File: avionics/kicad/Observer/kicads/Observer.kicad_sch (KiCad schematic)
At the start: 66 parts, among them Q1 AO3400 logic-level N-MOSFET, T1 Wurth 749010012A, T1_CMC1 SRF2012-100Y, T1_CMC2 SRF2012-100Y, T1_D1 PRTR5V0U2X, T1_D2 PRTR5V0U2X, T2 Wurth 749010012A, T2_CMC1 SRF2012-100Y, T2_CMC2 SRF2012-100Y, T2_D1 PRTR5V0U2X, T2_D2 PRTR5V0U2X, U2 Microchip KSZ9477, U3 TI MSPM0G3519-Q1, U4 TI ISOW1044BDFMR, U5 Infineon SLB 9672AU2.0, U6 TI ISOW1412, Y1 25MHz

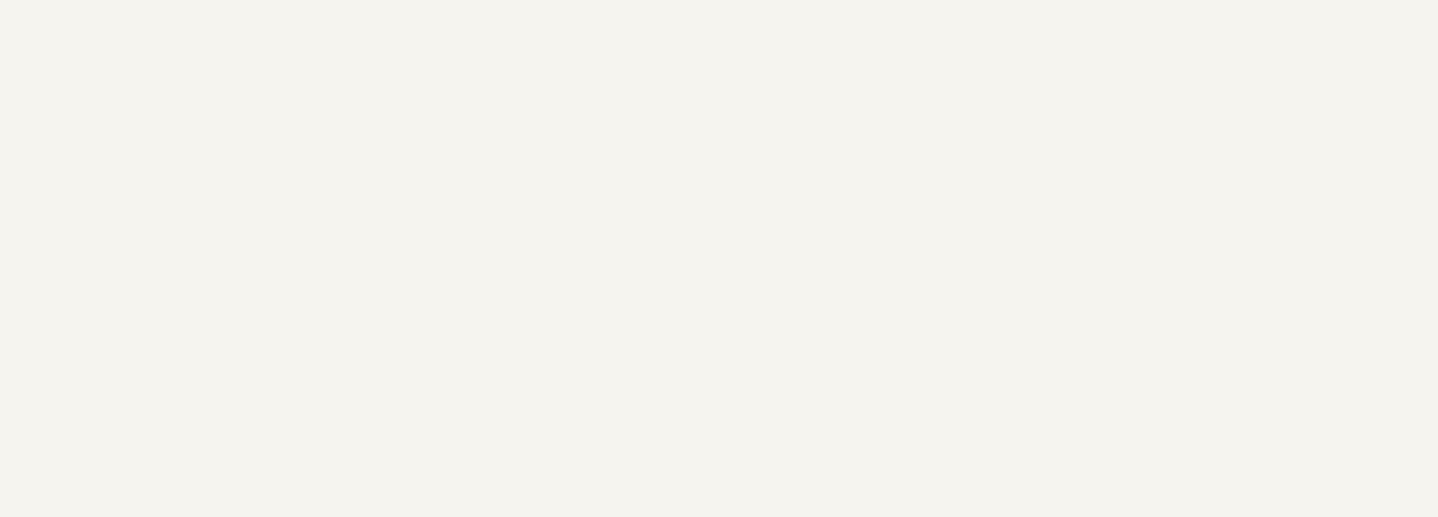
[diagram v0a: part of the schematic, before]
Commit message: docs(avionics): Wurth usage notice + uncrewed-only statement on 5 boards; catalogue REF-SENSOR-022..040
Owner decision 2026-09-26: retain the Wurth parts. The Wurth datasheet
usage notice is quoted verbatim [REF-SENSOR-028: Wurth 749010012A data
sheet rev 004.000 p.1] with an 'intended for use only on uncrewed
aircraft' statement in each Wurth-bearing board's .md, as a schematic
text item and PCB Cmts.User text, and in title-block comments 8/9
(tools/add_board_notices.py, idempotent). ERC/DRC/parity counts
unchanged on all five boards (kicad-cli 9.0.2).

REFERENCES.md: REF-SENSOR-022/023/025-030/033/038/040 were cited by
board schematics and generator scripts but never catalogued; entries
added with URLs validated 2026-09-26, unreachable ones marked
'requires verification'.

AI-authored: Claude Opus 5.5 (Anthropic).

Co-Authored-By: Claude Opus 5.5 <noreply@anthropic.com>
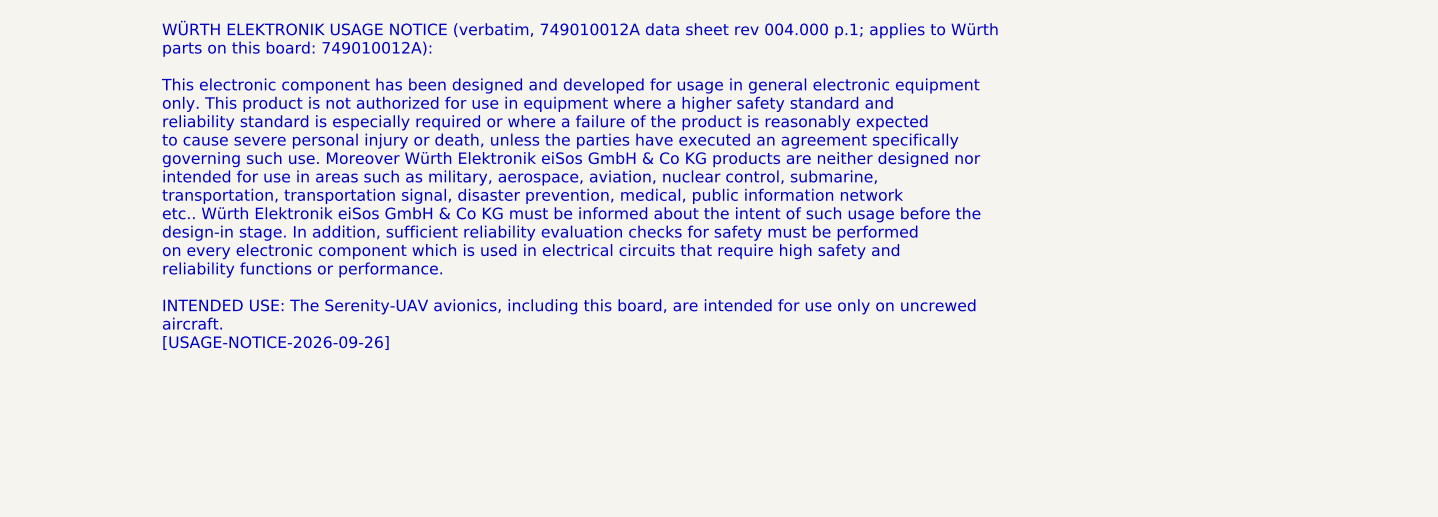
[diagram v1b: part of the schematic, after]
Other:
- note added: "WÜRTH ELEKTRONIK USAGE NOTICE (verbatim, 749010012A data sheet rev 004.000 p.1; applies to Würth parts on this board: 749010012A): This electronic component has been designed and developed for usage in general electronic equipment only. This product is not authorized for use in equipment where a higher safety standard and reliability standard is especially required or where a failure of the produ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"
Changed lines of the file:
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@@
     (comment 3 "License: CC BY 4.0  |  creativecommons.org/licenses/by/4.0")
     (comment 4 "SoM carrier: real clean-room symbols; see gen_Observer_carrier_sch.py")
-  )
+		(comment 8 "Wurth parts (749010012A): see Wurth usage notice on this page [USAGE-NOTICE-2026-09-26]")
+		(comment 9 "Intended for use ONLY on uncrewed aircraft")
+	)
   (text "OBSERVER — Nose/Cargo Vision/ToF/Laser  |  STANDALONE board (NOT a PB2-I cape)  |  SoM end-state: PHYTEC PCM-071 + carrier (KSZ9477 / MSPM0G3519-Q1 / SLB9672 / ISOW1044)" (at 10.00 8.00 0)
     (effects (font (size 2.00 2.00)))
@@
     (property "Intersheet References" "${INTERSHEET_REFS}" (at 137.16 195.58 0)
       (effects (font (size 1.016 1.016)) (hide yes))))
-)
+	(text "WÜRTH ELEKTRONIK USAGE NOTICE (verbatim, 749010012A data sheet rev 004.000 p.1; applies to Würth\nparts on this board: 749010012A):\n\nThis electronic component has been designed and developed for usage in general electronic equipment\nonly. This product is not authorized for use in equipment where a higher safety standard and\nreliability standard is especially required or where a failure of the product is reasonably expected\nto cause severe personal injury or death, unless the parties have executed an agreement specifically\ngoverning such use. Moreover Würth Elektronik eiSos GmbH & Co KG products are neither designed nor\nintended for use in areas such as military, aerospace, aviation, nuclear control, submarine,\ntransportation, transportation signal, disaster prevention, medical, public information network\netc.. Würth Elektronik eiSos GmbH & Co KG must be informed about the intent of such usage before the\ndesign-in stage. In addition, sufficient reliability evaluation checks for safety must be performed\non every electronic component which is used in electrical circuits that require high safety and\nreliability functions or performance.\n\nINTENDED USE: The Serenity-UAV avionics, including this board, are intended for use only on uncrewed\naircraft.\n[USAGE-NOTICE-2026-09-26]"
+		(exclude_from_sim no)
+		(at -35.56 -114.30 0)
+		(effects (font (size 1.27 1.27)) (justify left top))
+	)
+	)

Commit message: fix(avionics): TLV62569 -> TLV62569PDRLR and TLV75725 -> TLV75725PDRVR package swaps; regulator circuit fixes; stale-component cleanup
Owner-approved swaps (2026-09-26, avionics/WBS.md U7.1e) using the
datasheet-verified SecureControllers library via ${SECURE_CONTROLLERS_LIB}:
- CAN-PERIPH-GW-1 U_REG_3V3, Observer U_REG_3V3/U_REG_1V2, Flight
  Engineer U_REG_3V3_H -> TLV62569PDRLR (SOT-563, 1.6 x 1.6 mm).
  Pins remapped by name; the old symbols had FB/PG swapped (gateway,
  Observer) or sat on a 3-pad SOT-23 (Flight Engineer).
- Observer U_REG_2V5 -> TLV75725PDRVR (WSON-6 2x2, EP to GND).
- Feedback dividers per TLV62569 Sec. 8.2.2.2 Eq. 2 (VFB 0.6 V):
  gateway 10k/20k (0.9 V!) -> 453k/100k = 3.318 V; Observer placeholders
  -> 453k/100k (3V3) and 100k/100k (1V2).
- Flight Engineer: EN was tied to its own 3V3 output and FB straight to
  +3V3 (would regulate at 0.6 V); EN -> +5V, added R_H_FBT 453k /
  R_H_FBB 100k. Parity 2 -> 0, ERC 0.
- tools/kicad_prune_stale.py: parity-driven removal of stale electrical
  footprints and only the copper they orphan; mounting holes are marked
  board_only + renumbered (Commo parity 93 -> 86, Observer 21 -> 17).
- New tools kicad_relink.py / kicad_add_part.py / kicad_set_value.py;
  SecureControllers entries added to every board's lib tables.

Sources: TI TLV62569 (SLVSDG1C) Pin Functions, Sec. 8.2.2.2; TI TLV757P
Fig. 4-3, Pin Functions, DRV0006A.

AI-authored: Claude Opus 5.5 (Anthropic).

Co-Authored-By: Claude Opus 5.5 <noreply@anthropic.com>
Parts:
- R_FB1B, R_FB3B: value R_fbbot -> 100k 1%
- R_FB1T: value R_fbtop -> 100k 1%
- R_FB3T: value R_fbtop -> 453k 1%
- U_REG_1V2: value TLV62569 -> +1V2 -> TLV62569PDRLR; footprint Package_TO_SOT_SMD:SOT-23-6 -> Package_TO_SOT_SMD:SOT-563; symbol TLV62569_DBV -> SecureControllers:TLV62569PDRL
- U_REG_2V5: value TLV75725 -> +2V5 -> TLV75725PDRVR; footprint Package_TO_SOT_SMD:SOT-23-5 -> Package_SON:WSON-6-1EP_2x2mm_P0.65mm_EP1x1.6mm; symbol TLV75725_DBV -> SecureControllers:TLV75725PDRV
- U_REG_3V3: value TLV62569 -> +3V3 -> TLV62569PDRLR; footprint Package_TO_SOT_SMD:SOT-23-6 -> Package_TO_SOT_SMD:SOT-563; symbol TLV62569_DBV -> SecureControllers:TLV62569PDRL
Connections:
- net +2V5: now also U_REG_2V5.1 (OUT); no longer U_REG_2V5.5 (OUT)
- net +3V3: now also U_REG_2V5.4 (EN), U_REG_2V5.6 (IN); no longer U_REG_2V5.1 (IN), U_REG_2V5.3 (EN)
- net +5V: now also U_REG_1V2.3 (VIN), U_REG_1V2.5 (EN), U_REG_3V3.3 (VIN), U_REG_3V3.5 (EN); no longer U_REG_1V2.1 (EN), U_REG_1V2.4 (VIN), U_REG_3V3.1 (EN), U_REG_3V3.4 (VIN)
- net GND: now also U_REG_2V5.3 (GND), U_REG_2V5.7 (EP); no longer U_REG_2V5.2 (GND)
- net U_REG_1V2_FB: now also U_REG_1V2.1 (FB); no longer U_REG_1V2.5 (FB)
- net U_REG_1V2_SW: now also U_REG_1V2.4 (SW); no longer U_REG_1V2.3 (SW)
- net U_REG_3V3_FB: now also U_REG_3V3.1 (FB); no longer U_REG_3V3.5 (FB)
- net U_REG_3V3_SW: now also U_REG_3V3.4 (SW); no longer U_REG_3V3.3 (SW)
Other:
- moved on the sheet: U_REG_1V2, U_REG_3V3
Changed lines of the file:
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@@
     (property "Intersheet References" "${INTERSHEET_REFS}" (at 19.92 33.27 0)
       (effects (font (size 1.016 1.016)) (hide yes))))
-  (symbol (lib_id "TLV62569_DBV") (at 25.00 48.00 0)
+  (symbol (lib_id "SecureControllers:TLV62569PDRL") (at 25.00 48.00 0)
     (unit 1) (exclude_from_sim no) (in_bom yes) (on_board yes) (dnp no)
     (property "Reference" "U_REG_3V3" (at 25.00 44.19 0)
       (effects (font (size 1.27 1.27))))
-    (property "Value" "TLV62569 -> +3V3" (at 25.00 51.81 0)
-      (effects (font (size 1.27 1.27))))
-    (property "Footprint" "Package_TO_SOT_SMD:SOT-23-6" (at 0 0 0)
-      (effects (font (size 1.27 1.27)) (hide yes)))
-    (property "Datasheet" "" (at 0 0 0)
-      (effects (font (size 1.27 1.27)) (hide yes)))
-  )
-  (global_label "+5V" (shape bidirectional) (at 17.38 45.46 180)
+    (property "Value" "TLV62569PDRLR" (at 25.00 51.81 0)
+      (effects (font (size 1.27 1.27))))
+    (property "Footprint" "Package_TO_SOT_SMD:SOT-563" (at 0 0 0)
+      (effects (font (size 1.27 1.27)) (hide yes)))
+    (property "Datasheet" "https://www.ti.com/lit/ds/symlink/tlv62569.pdf" (at 0 0 0)
+      (effects (font (size 1.27 1.27)) (hide yes)))
+  )
+  (global_label "+5V" (shape bidirectional) (at 14.8400 45.4600 180)
     (effects (font (size 1.016 1.016)))
     (property "Intersheet References" "${INTERSHEET_REFS}" (at 17.38 45.46 0)
       (effects (font (size 1.016 1.016)) (hide yes))))
-  (global_label "GND" (shape bidirectional) (at 17.38 48.00 180)
+  (global_label "GND" (shape bidirectional) (at 25.0000 58.1600 270)
     (effects (font (size 1.016 1.016)))
     (property "Intersheet References" "${INTERSHEET_REFS}" (at 17.38 48.00 0)
       (effects (font (size 1.016 1.016)) (hide yes))))
-  (global_label "+5V" (shape bidirectional) (at 17.38 50.54 180)
+  (global_label "+5V" (shape bidirectional) (at 14.8400 42.9200 180)
     (effects (font (size 1.016 1.016)))
     (property "Intersheet References" "${INTERSHEET_REFS}" (at 17.38 50.54 0)
       (effects (font (size 1.016 1.016)) (hide yes))))
-  (global_label "U_REG_3V3_SW" (shape bidirectional) (at 32.62 45.46 0)
+  (global_label "U_REG_3V3_SW" (shape bidirectional) (at 35.1600 42.9200 0)
     (effects (font (size 1.016 1.016)))
     (property "Intersheet References" "${INTERSHEET_REFS}" (at 32.62 45.46 0)
       (effects (font (size 1.016 1.016)) (hide yes))))
-  (global_label "U_REG_3V3_FB" (shape bidirectional) (at 32.62 48.00 0)
+  (global_label "U_REG_3V3_FB" (shape bidirectional) (at 35.1600 45.4600 0)
     (effects (font (size 1.016 1.016)))
     (property "Intersheet References" "${INTERSHEET_REFS}" (at 32.62 48.00 0)
       (effects (font (size 1.016 1.016)) (hide yes))))
-  (global_label "+3V3_PG" (shape bidirectional) (at 32.62 50.54 0)
+  (global_label "+3V3_PG" (shape bidirectional) (at 35.1600 48.0000 0)
     (effects (font (size 1.016 1.016)))
     (property "Intersheet References" "${INTERSHEET_REFS}" (at 32.62 50.54 0)
@@
     (property "Reference" "R_FB3T" (at 45.00 50.19 0)
       (effects (font (size 1.27 1.27))))
-    (property "Value" "R_fbtop" (at 45.00 57.81 0)
+    (property "Value" "453k 1%" (at 45.00 57.81 0)
       (effects (font (size 1.27 1.27))))
     (property "Footprint" "Resistor_SMD:R_0402_1005Metric" (at 0 0 0)
@@
     (property "Reference" "R_FB3B" (at 45.00 55.19 0)
       (effects (font (size 1.27 1.27))))
-    (property "Value" "R_fbbot" (at 45.00 62.81 0)
+    (property "Value" "100k 1%" (at 45.00 62.81 0)
       (effects (font (size 1.27 1.27))))
     (property "Footprint" "Resistor_SMD:R_0402_1005Metric" (at 0 0 0)
@@
     (property "Intersheet References" "${INTERSHEET_REFS}" (at 12.81 48.00 0)
       (effects (font (size 1.016 1.016)) (hide yes))))
-  (symbol (lib_id "TLV62569_DBV") (at 25.00 70.00 0)
+  (symbol (lib_id "SecureControllers:TLV62569PDRL") (at 25.00 70.00 0)
     (unit 1) (exclude_from_sim no) (in_bom yes) (on_board yes) (dnp no)
     (property "Reference" "U_REG_1V2" (at 25.00 66.19 0)
       (effects (font (size 1.27 1.27))))
-    (property "Value" "TLV62569 -> +1V2" (at 25.00 73.81 0)
-      (effects (font (size 1.27 1.27))))
-    (property "Footprint" "Package_TO_SOT_SMD:SOT-23-6" (at 0 0 0)
-      (effects (font (size 1.27 1.27)) (hide yes)))
-    (property "Datasheet" "" (at 0 0 0)
-      (effects (font (size 1.27 1.27)) (hide yes)))
-  )
-  (global_label "+5V" (shape bidirectional) (at 17.38 67.46 180)
+    (property "Value" "TLV62569PDRLR" (at 25.00 73.81 0)
+      (effects (font (size 1.27 1.27))))
+    (property "Footprint" "Package_TO_SOT_SMD:SOT-563" (at 0 0 0)
+      (effects (font (size 1.27 1.27)) (hide yes)))
+    (property "Datasheet" "https://www.ti.com/lit/ds/symlink/tlv62569.pdf" (at 0 0 0)
+      (effects (font (size 1.27 1.27)) (hide yes)))
+  )
+  (global_label "+5V" (shape bidirectional) (at 14.8400 67.4600 180)
     (effects (font (size 1.016 1.016)))
     (property "Intersheet References" "${INTERSHEET_REFS}" (at 17.38 67.46 0)
       (effects (font (size 1.016 1.016)) (hide yes))))
-  (global_label "GND" (shape bidirectional) (at 17.38 70.00 180)
+  (global_label "GND" (shape bidirectional) (at 25.0000 80.1600 270)
     (effects (font (size 1.016 1.016)))
     (property "Intersheet References" "${INTERSHEET_REFS}" (at 17.38 70.00 0)
       (effects (font (size 1.016 1.016)) (hide yes))))
-  (global_label "+5V" (shape bidirectional) (at 17.38 72.54 180)
+  (global_label "+5V" (shape bidirectional) (at 14.8400 64.9200 180)
     (effects (font (size 1.016 1.016)))
     (property "Intersheet References" "${INTERSHEET_REFS}" (at 17.38 72.54 0)
       (effects (font (size 1.016 1.016)) (hide yes))))
-  (global_label "U_REG_1V2_SW" (shape bidirectional) (at 32.62 67.46 0)
+  (global_label "U_REG_1V2_SW" (shape bidirectional) (at 35.1600 64.9200 0)
     (effects (font (size 1.016 1.016)))
     (property "Intersheet References" "${INTERSHEET_REFS}" (at 32.62 67.46 0)
       (effects (font (size 1.016 1.016)) (hide yes))))
-  (global_label "U_REG_1V2_FB" (shape bidirectional) (at 32.62 70.00 0)
+  (global_label "U_REG_1V2_FB" (shape bidirectional) (at 35.1600 67.4600 0)
     (effects (font (size 1.016 1.016)))
     (property "Intersheet References" "${INTERSHEET_REFS}" (at 32.62 70.00 0)
       (effects (font (size 1.016 1.016)) (hide yes))))
-  (global_label "+1V2_PG" (shape bidirectional) (at 32.62 72.54 0)
+  (global_label "+1V2_PG" (shape bidirectional) (at 35.1600 70.0000 0)
     (effects (font (size 1.016 1.016)))
     (property "Intersheet References" "${INTERSHEET_REFS}" (at 32.62 72.54 0)
@@
     (property "Reference" "R_FB1T" (at 45.00 72.19 0)
       (effects (font (size 1.27 1.27))))
-    (property "Value" "R_fbtop" (at 45.00 79.81 0)
+    (property "Value" "100k 1%" (at 45.00 79.81 0)
       (effects (font (size 1.27 1.27))))
     (property "Footprint" "Resistor_SMD:R_0402_1005Metric" (at 0 0 0)
@@
     (property "Reference" "R_FB1B" (at 45.00 77.19 0)
       (effects (font (size 1.27 1.27))))
-    (property "Value" "R_fbbot" (at 45.00 84.81 0)
+    (property "Value" "100k 1%" (at 45.00 84.81 0)
       (effects (font (size 1.27 1.27))))
     (property "Footprint" "Resistor_SMD:R_0402_1005Metric" (at 0 0 0)
@@
     (property "Intersheet References" "${INTERSHEET_REFS}" (at 12.81 70.00 0)
       (effects (font (size 1.016 1.016)) (hide yes))))
-  (symbol (lib_id "TLV75725_DBV") (at 90.00 48.00 0)
+  (symbol (lib_id "SecureControllers:TLV75725PDRV") (at 90.00 48.00 0)
     (unit 1) (exclude_from_sim no) (in_bom yes) (on_board yes) (dnp no)
     (property "Reference" "U_REG_2V5" (at 90.00 44.19 0)
       (effects (font (size 1.27 1.27))))
-    (property "Value" "TLV75725 -> +2V5" (at 90.00 51.81 0)
-      (effects (font (size 1.27 1.27))))
-    (property "Footprint" "Package_TO_SOT_SMD:SOT-23-5" (at 0 0 0)
-      (effects (font (size 1.27 1.27)) (hide yes)))
-    (property "Datasheet" "" (at 0 0 0)
-      (effects (font (size 1.27 1.27)) (hide yes)))
-  )
-  (global_label "+3V3" (shape bidirectional) (at 82.38 45.46 180)
+    (property "Value" "TLV75725PDRVR" (at 90.00 51.81 0)
+      (effects (font (size 1.27 1.27))))
+    (property "Footprint" "Package_SON:WSON-6-1EP_2x2mm_P0.65mm_EP1x1.6mm" (at 0 0 0)
+      (effects (font (size 1.27 1.27)) (hide yes)))
+    (property "Datasheet" "https://www.ti.com/lit/ds/symlink/tlv757p.pdf" (at 0 0 0)
+      (effects (font (size 1.27 1.27)) (hide yes)))
+  )
+  (global_label "+3V3" (shape bidirectional) (at 79.8400 42.9200 180)
     (effects (font (size 1.016 1.016)))
     (property "Intersheet References" "${INTERSHEET_REFS}" (at 82.38 45.46 0)
       (effects (font (size 1.016 1.016)) (hide yes))))
-  (global_label "GND" (shape bidirectional) (at 82.38 48.00 180)
+  (global_label "GND" (shape bidirectional) (at 87.4600 58.1600 270)
     (effects (font (size 1.016 1.016)))
     (property "Intersheet References" "${INTERSHEET_REFS}" (at 82.38 48.00 0)
       (effects (font (size 1.016 1.016)) (hide yes))))
-  (global_label "+3V3" (shape bidirectional) (at 82.38 50.54 180)
+  (global_label "+3V3" (shape bidirectional) (at 79.8400 45.4600 180)
     (effects (font (size 1.016 1.016)))
     (property "Intersheet References" "${INTERSHEET_REFS}" (at 82.38 50.54 0)
       (effects (font (size 1.016 1.016)) (hide yes))))
-  (global_label "+2V5" (shape bidirectional) (at 97.62 48.00 0)
+  (global_label "+2V5" (shape bidirectional) (at 100.1600 42.9200 0)
     (effects (font (size 1.016 1.016)))
     (property "Intersheet References" "${INTERSHEET_REFS}" (at 97.62 48.00 0)
@@
 		(effects (font (size 1.27 1.27)) (justify left top))
 	)
-	)
+	(global_label "GND" (shape bidirectional) (at 90.0000 58.1600 270)
+    (effects (font (size 1.27 1.27)))
+)
+  )
